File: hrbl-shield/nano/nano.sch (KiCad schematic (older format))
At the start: 44 parts, among them P1 Digital, P2 Analog, P3 CONN_01X01, P4 CONN_01X01, P5 CONN_01X01, P6 CONN_01X01, U1 4N25, U10 4N25, U11 4N25, U12 4N25, U13 4N25, U14 74AHC1G14, U15 AMS1117-5.0, U2 4N25, U3 4N25, U4 4N25, U5 4N25, U6 4N25, U7 4N25, U8 4N25, U9 4N25, Y1_PLUG_SOCKET1 Conn_01x08, Y2_PLUG_SOCKET1 Conn_01x08

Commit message: Updated nano card
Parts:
- removed R?: 3k, Resistor_SMD:R_1206_3216Metric_Pad1.42x1.75mm_HandSolder, symbol Device:R
- removed U14: 74AHC1G14, symbol 74xGxx:74AHC1G14
- removed U15: AMS1117-5.0, Package_TO_SOT_SMD:SOT-223-3_TabPin2, symbol Regulator_Linear:AMS1117-5.0
- removed U?: 4N25, Package_DIP:DIP-6_W7.62mm, symbol Isolator:4N25
- added C1: 10uF, Capacitor_SMD:C_1206_3216Metric_Pad1.42x1.75mm_HandSolder, symbol pspice:CAP
- added C2, C3: 100nF (0.1uF), Capacitor_SMD:C_1206_3216Metric_Pad1.42x1.75mm_HandSolder, symbol pspice:CAP
- added R15: 220, Resistor_SMD:R_1206_3216Metric_Pad1.42x1.75mm_HandSolder, symbol Device:R
- added U14, U16: 4N25, Package_DIP:DIP-6_W7.62mm, symbol Isolator:4N25
- added U15: IFX27001TFV50ATMA1CT-ND, Package_TO_SOT_SMD:TO-252-3_TabPin2, symbol Regulator_Linear:IFX27001TFV50ATMA1CT-ND
- POWER_IN1, PROBE1: footprint (none) -> Connector_Phoenix_MC:PhoenixContact_MCV_1,5_2-G-3.81_1x02_P3.81mm_Vertical
- R13: value 20k -> 220
- SPINDLE_CTR1: footprint (none) -> Connector_Phoenix_MC:PhoenixContact_MCV_1,5_4-G-3.81_1x04_P3.81mm_Vertical
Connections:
- wire segments 84 -> 100
- no-connect marks 30 -> 31
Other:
- note added: "Acc manual: \nR min 460 ohm\n"
- note added: "All IN PINs\nhas internal 20k \npull up resistor to +5V"
- note added: "All motors ALARM in Parallell"
- note added: "Potential ground loop with spindle case earth"
- note added: "Reset on loss of external power. Two coupers to invert signal\n"
- note added: "Will act as shorted pull down all the time"
- note removed: "ABORT has internal 20k pull up resistor to +5V"
- note removed: "Buck coverter?\n"
- note removed: "Check this"
- note removed: "Reset on loss of external power"
- note removed: "This grounds GNDPWR and GNDS"
- moved on the sheet: PROBE1, R1, R10, R11, R14, R2, R3, R4, R5, R6, R7, R8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

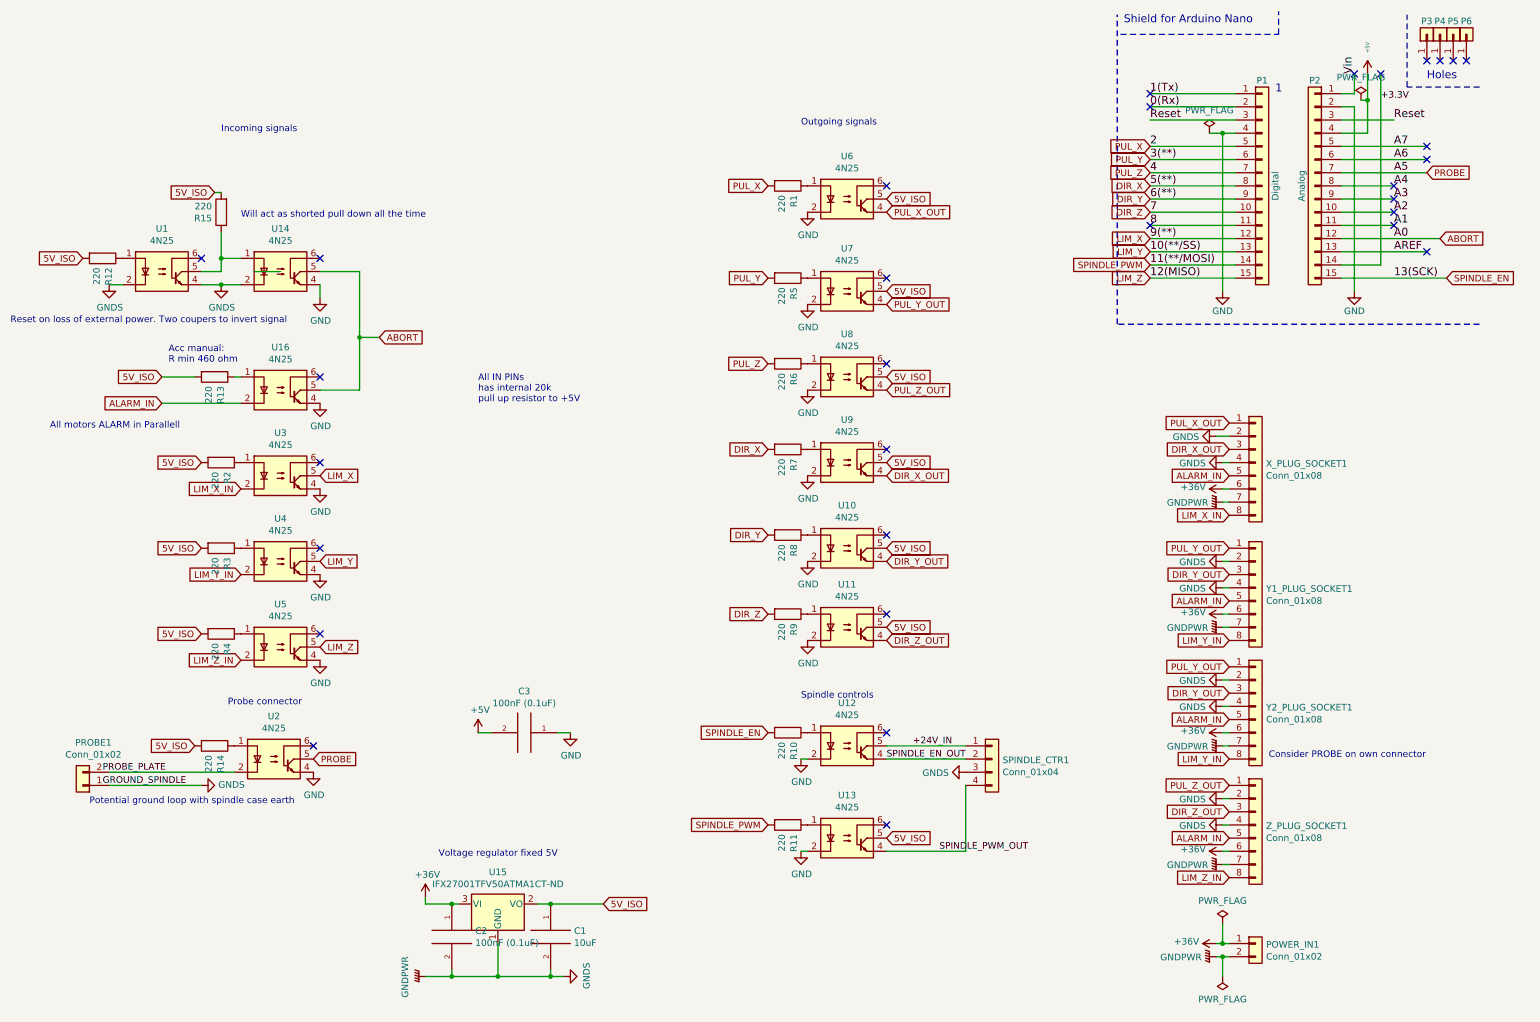
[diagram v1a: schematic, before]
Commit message: Updated nano card
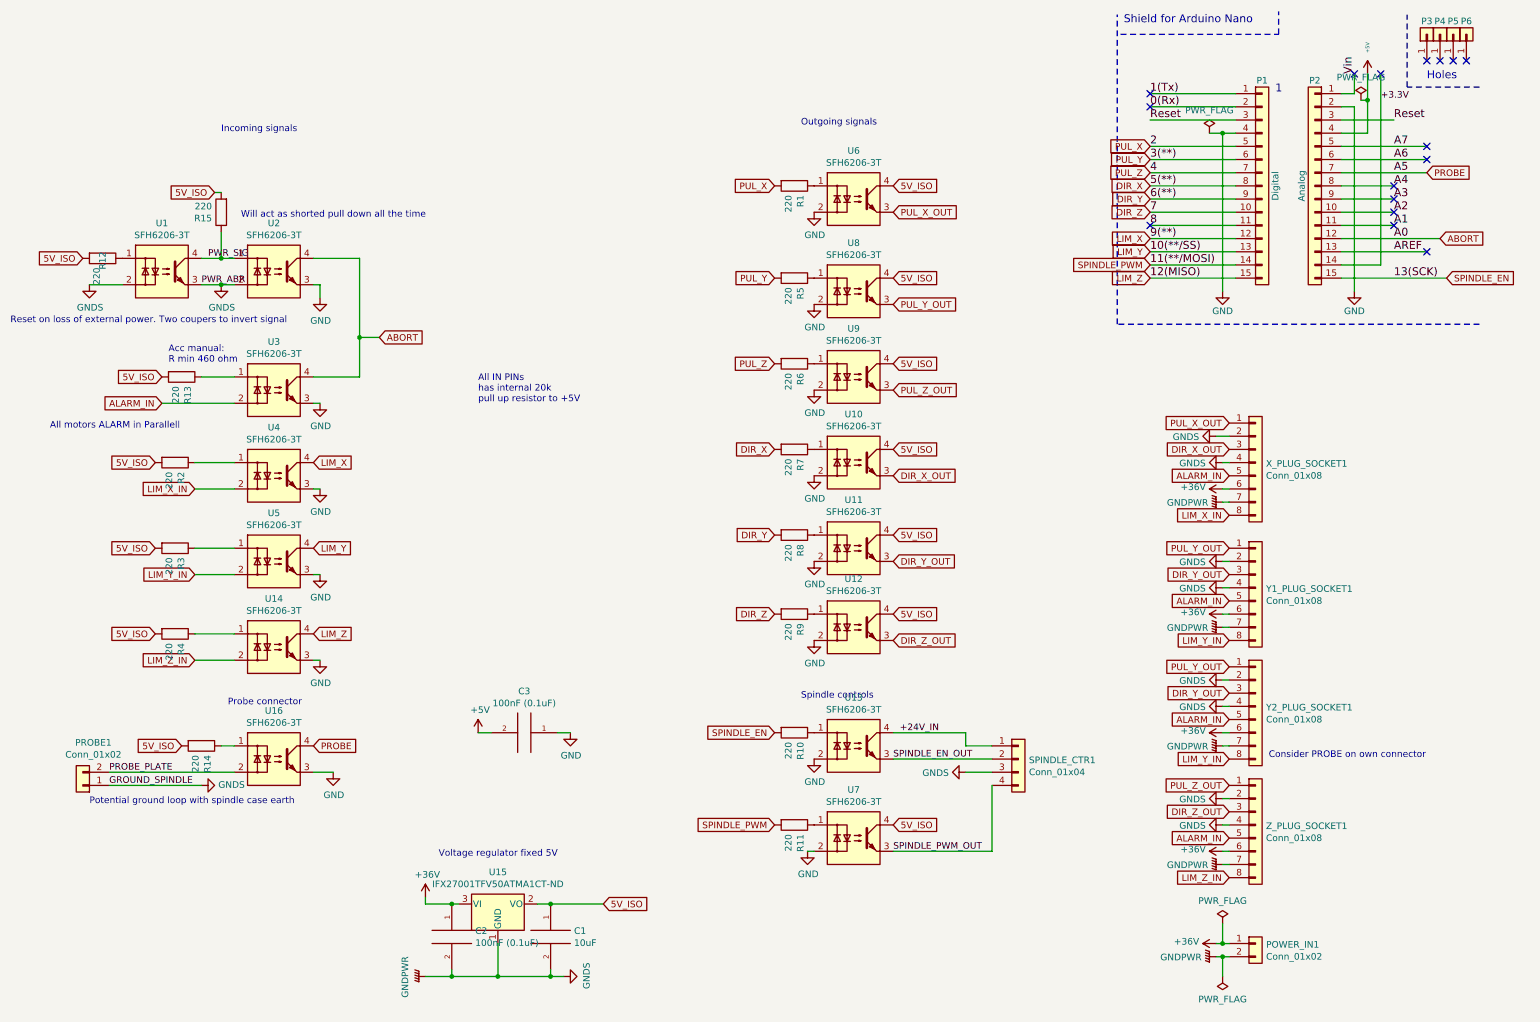
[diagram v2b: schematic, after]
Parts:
- removed U1, U10, U11, U12, U13, U14, U16, U2, U3, U4, U5, U6, U7, U8, U9: 4N25, Package_DIP:DIP-6_W7.62mm, symbol Isolator:4N25
- added U1, U10, U11, U12, U13, U14, U16, U2, U3, U4, U5, U6, U7, U8, U9: SFH6206-3T, Package_DIP:SMDIP-4_W9.53mm_Clearance8mm, symbol Isolator:SFH6206-3T
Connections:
- net +24V_IN: now also U13.4
- net 5V_ISO: now also U10.4, U11.4, U12.4, U6.4, U7.4, U8.4, U9.4
- net ABORT: now also U2.4, U3.4
- net ALARM_IN: now also U3.2
- net DIR_X_OUT: now also U10.3
- net DIR_Y_OUT: now also U11.3
- net DIR_Z_OUT: now also U12.3
- net GND: now also U10.2, U11.2, U12.2, U13.2, U14.3, U16.3, U2.3, U3.3, U4.3, U5.3, U6.2, U7.2, U8.2, U9.2
- net GNDPWR: now also U1.2, U1.3, U2.2
- net LIM_X: now also U4.4
- net LIM_X_IN: now also U4.2
- net LIM_Y: now also U5.4
- net LIM_Y_IN: now also U5.2
- net LIM_Z: now also U14.4
- net LIM_Z_IN: now also U14.2
- net PROBE: now also U16.4
- net PROBE_PLATE: now also PROBE1.2 (Pin_2), U16.2
- net PUL_X_OUT: now also U6.3
- net PUL_Y_OUT: now also U8.3
- net PUL_Z_OUT: now also U9.3
- net SPINDLE_EN_OUT: now also U13.3
- net SPINDLE_PWM_OUT: now also U7.3
- net at R1.1: now also U6.1
- net at R14.1: now also U16.1
- net at R2.1: now also U4.1
- net at R3.1: now also U5.1
- net at R4.1: now also U14.1
- net at R5.1: now also U8.1
- net at R6.1: now also U9.1
- net at R7.1: now also U10.1
- net at R8.1: now also U11.1
- net at R9.1: now also U12.1
- net at R10.1: now also U13.1
- net at R11.1: now also U7.1
- net at R12.1: now also U1.1
- net PWR_SIG: now reaches R15.1
- net PWR_SIG: now also U1.4, U2.1
- net at R13.1: now also U3.1
- no-connect marks 31 -> 16
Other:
- moved on the sheet: R1, R10, R11, R13, R14, R2, R3, R4, R5, R6, R7, R8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

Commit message: Updated nano sheild
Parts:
- added R16, R17, R18, R19: 0, Resistor_SMD:R_1206_3216Metric_Pad1.42x1.75mm_HandSolder, symbol Device:R
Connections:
- net ALARM_IN: now also R16.1, R16.2, R17.1, R17.2, R18.1, R18.2
- net PUL_Z_OUT: now also R19.1; no longer U9.3
- new net: R19.2, U9.3
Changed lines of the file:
@@
 	1    0    0    -1
 $EndComp
-Text GLabel 6750 3350 2    50   Input ~ 0
+Text GLabel 7250 3350 2    50   Input ~ 0
 PUL_Z_OUT
 Text GLabel 6750 3150 2    50   Input ~ 0
@@
 Text GLabel 9300 3800 0    50   Input ~ 0
 DIR_X_OUT
-Text GLabel 9300 4000 0    50   Input ~ 0
+Text GLabel 9000 4000 0    50   Input ~ 0
 ALARM_IN
 Text GLabel 9300 4300 0    50   Input ~ 0
@@
 Text GLabel 9300 4750 0    50   Input ~ 0
 DIR_Y_OUT
-Text GLabel 9300 4950 0    50   Input ~ 0
+Text GLabel 9000 4950 0    50   Input ~ 0
 ALARM_IN
 Text GLabel 9300 5250 0    50   Input ~ 0
@@
 Text GLabel 9300 6550 0    50   Input ~ 0
 DIR_Z_OUT
-Text GLabel 9300 6750 0    50   Input ~ 0
+Text GLabel 9000 6750 0    50   Input ~ 0
 ALARM_IN
 Text GLabel 9300 7050 0    50   Input ~ 0
@@
 Connection ~ 3750 7800
 Connection ~ 4150 7800
+$Comp
+L Device:R R16
+U 1 1 5B865306
+P 9150 4000
+F 0 "R16" V 8943 4000 50  0000 C CNN
+F 1 "0" V 9034 4000 50  0000 C CNN
+F 2 "Resistor_SMD:R_1206_3216Metric_Pad1.42x1.75mm_HandSolder" V 9080 4000 50  0001 C CNN
+F 3 "~" H 9150 4000 50  0001 C CNN
+	1    9150 4000
+	0    1    1    0
+$EndComp
+$Comp
+L power:GNDS #PWR0111
+U 1 1 5B865792
+P 8850 4900
+F 0 "#PWR0111" H 8850 4650 50  0001 C CNN
+F 1 "GNDS" V 8855 4772 50  0000 R CNN
+F 2 "" H 8850 4900 50  0001 C CNN
+F 3 "" H 8850 4900 50  0001 C CNN
+	1    8850 4900
+	0    1    1    0
+$EndComp
+$Comp
+L power:GNDS #PWR0112
+U 1 1 5B86BCA7
+P 9050 6650
+F 0 "#PWR0112" H 9050 6400 50  0001 C CNN
+F 1 "GNDS" V 9055 6522 50  0000 R CNN
+F 2 "" H 9050 6650 50  0001 C CNN
+F 3 "" H 9050 6650 50  0001 C CNN
+	1    9050 6650
+	0    1    1    0
+$EndComp
+$Comp
+L Device:R R18
+U 1 1 5B86BCAD
+P 9150 6750
+F 0 "R18" V 8943 6750 50  0000 C CNN
+F 1 "0" V 9034 6750 50  0000 C CNN
+F 2 "Resistor_SMD:R_1206_3216Metric_Pad1.42x1.75mm_HandSolder" V 9080 6750 50  0001 C CNN
+F 3 "~" H 9150 6750 50  0001 C CNN
+	1    9150 6750
+	0    1    1    0
+$EndComp
+Wire Wire Line
+	9300 6750 9000 6750
+Connection ~ 9300 6750
+$Comp
+L Device:R R17
+U 1 1 5B865798
+P 9150 4950
+F 0 "R17" V 8943 4950 50  0000 C CNN
+F 1 "0" V 9034 4950 50  0000 C CNN
+F 2 "Resistor_SMD:R_1206_3216Metric_Pad1.42x1.75mm_HandSolder" V 9080 4950 50  0001 C CNN
+F 3 "~" H 9150 4950 50  0001 C CNN
+	1    9150 4950
+	0    1    1    0
+$EndComp
+Connection ~ 9300 4000
+Wire Wire Line
+	9000 4000 9300 4000
+Connection ~ 9300 4950
+Wire Wire Line
+	9000 4950 9300 4950
+$Comp
+L power:GNDS #PWR0113
+U 1 1 5B886EF5
+P 7000 3400
+F 0 "#PWR0113" H 7000 3150 50  0001 C CNN
+F 1 "GNDS" V 7005 3272 50  0000 R CNN
+F 2 "" H 7000 3400 50  0001 C CNN
+F 3 "" H 7000 3400 50  0001 C CNN
+	1    7000 3400
+	0    1    1    0
+$EndComp
+$Comp
+L Device:R R19
+U 1 1 5B886EFB
+P 6950 3350
+F 0 "R19" V 6743 3350 50  0000 C CNN
+F 1 "0" V 6834 3350 50  0000 C CNN
+F 2 "Resistor_SMD:R_1206_3216Metric_Pad1.42x1.75mm_HandSolder" V 6880 3350 50  0001 C CNN
+F 3 "~" H 6950 3350 50  0001 C CNN
+	1    6950 3350
+	0    1    1    0
+$EndComp
+Wire Wire Line
+	6750 3350 6800 3350
+Wire Wire Line
+	7100 3350 7250 3350
 Wire Wire Line
 	3750 7800 4150 7800

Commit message: updated Nano shield
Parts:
- added R20: 0, Resistor_SMD:R_1206_3216Metric_Pad1.42x1.75mm_HandSolder, symbol Device:R
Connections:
- net GNDPWR: now also R20.2; no longer C1.2, PROBE1.1 (Pin_1), SPINDLE_CTR1.3 (Pin_3), U1.2, U1.3, U2.2, X_PLUG_SOCKET1.2 (Pin_2), X_PLUG_SOCKET1.4 (Pin_4), Y1_PLUG_SOCKET1.2 (Pin_2), Y1_PLUG_SOCKET1.4 (Pin_4), Y2_PLUG_SOCKET1.2 (Pin_2), Y2_PLUG_SOCKET1.4 (Pin_4), Z_PLUG_SOCKET1.2 (Pin_2), Z_PLUG_SOCKET1.4 (Pin_4)
- new net GNDS: C1.2, PROBE1.1 (Pin_1), R20.1, SPINDLE_CTR1.3 (Pin_3), U1.2, U1.3, U2.2, X_PLUG_SOCKET1.2 (Pin_2), X_PLUG_SOCKET1.4 (Pin_4), Y1_PLUG_SOCKET1.2 (Pin_2), Y1_PLUG_SOCKET1.4 (Pin_4), Y2_PLUG_SOCKET1.2 (Pin_2), Y2_PLUG_SOCKET1.4 (Pin_4), Z_PLUG_SOCKET1.2 (Pin_2), Z_PLUG_SOCKET1.4 (Pin_4)
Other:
- note added: "this 0 R is to control where the grounds join"
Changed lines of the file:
@@
 Text Label 1550 2350 0    50   ~ 0
 PWR_SIG
-Connection ~ 3750 7800
-Connection ~ 4150 7800
 $Comp
 L Device:R R16
@@
 Wire Wire Line
 	7100 3350 7250 3350
+$Comp
+L power:GNDS #PWR0114
+U 1 1 5B8A262D
+P 4050 7700
+F 0 "#PWR0114" H 4050 7450 50  0001 C CNN
+F 1 "GNDS" V 4055 7572 50  0000 R CNN
+F 2 "" H 4050 7700 50  0001 C CNN
+F 3 "" H 4050 7700 50  0001 C CNN
+	1    4050 7700
+	0    1    1    0
+$EndComp
+$Comp
+L Device:R R20
+U 1 1 5B8A2633
+P 3950 7800
+F 0 "R20" V 3743 7800 50  0000 C CNN
+F 1 "0" V 3834 7800 50  0000 C CNN
+F 2 "Resistor_SMD:R_1206_3216Metric_Pad1.42x1.75mm_HandSolder" V 3880 7800 50  0001 C CNN
+F 3 "~" H 3950 7800 50  0001 C CNN
+	1    3950 7800
+	0    1    1    0
+$EndComp
 Wire Wire Line
-	3750 7800 4150 7800
+	3800 7800 3750 7800
+Connection ~ 3750 7800
+Wire Wire Line
+	4100 7800 4150 7800
+Connection ~ 4150 7800
+Text Notes 3550 8000 0    50   ~ 0
+this 0 R is to control where the grounds join
 $EndSCHEMATC

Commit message: Nano sheild
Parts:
- added MH1, MH2, MH3, MH4: MountingHole, MountingHole:MountingHole_4.5mm_Pad, symbol Mechanical:MountingHole
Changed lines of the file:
@@
 Text Notes 3550 8000 0    50   ~ 0
 this 0 R is to control where the grounds join
+$Comp
+L Mechanical:MountingHole MH4
+U 1 1 5B8B75FD
+P 1700 7500
+F 0 "MH4" H 1800 7546 50  0000 L CNN
+F 1 "MountingHole" H 1800 7455 50  0000 L CNN
+F 2 "MountingHole:MountingHole_4.5mm_Pad" H 1700 7500 50  0001 C CNN
+F 3 "~" H 1700 7500 50  0001 C CNN
+	1    1700 7500
+	1    0    0    -1
+$EndComp
+$Comp
+L Mechanical:MountingHole MH3
+U 1 1 5B8B7AAF
+P 1350 7500
+F 0 "MH3" H 1450 7546 50  0000 L CNN
+F 1 "MountingHole" H 1450 7455 50  0000 L CNN
+F 2 "MountingHole:MountingHole_4.5mm_Pad" H 1350 7500 50  0001 C CNN
+F 3 "~" H 1350 7500 50  0001 C CNN
+	1    1350 7500
+	1    0    0    -1
+$EndComp
+$Comp
+L Mechanical:MountingHole MH2
+U 1 1 5B8B7CFB
+P 1050 7500
+F 0 "MH2" H 1150 7546 50  0000 L CNN
+F 1 "MountingHole" H 1150 7455 50  0000 L CNN
+F 2 "MountingHole:MountingHole_4.5mm_Pad" H 1050 7500 50  0001 C CNN
+F 3 "~" H 1050 7500 50  0001 C CNN
+	1    1050 7500
+	1    0    0    -1
+$EndComp
+$Comp
+L Mechanical:MountingHole MH1
+U 1 1 5B8B7D84
+P 700 7500
+F 0 "MH1" H 800 7546 50  0000 L CNN
+F 1 "MountingHole" H 800 7455 50  0000 L CNN
+F 2 "MountingHole:MountingHole_4.5mm_Pad" H 700 7500 50  0001 C CNN
+F 3 "~" H 700 7500 50  0001 C CNN
+	1    700  7500
+	1    0    0    -1
+$EndComp
 $EndSCHEMATC
